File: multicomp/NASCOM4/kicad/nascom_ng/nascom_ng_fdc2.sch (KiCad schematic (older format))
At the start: 32 parts, among them J12 Conn_02x01, J15 Conn_01x04_Male, J16 Conn_01x04_Male, J17 Conn_01x04_Male, J18 Conn_01x04_Male, U14 74LS38, U16 74HCT10, U17 74HCT123, U3 74LS06, U9 74HCT123

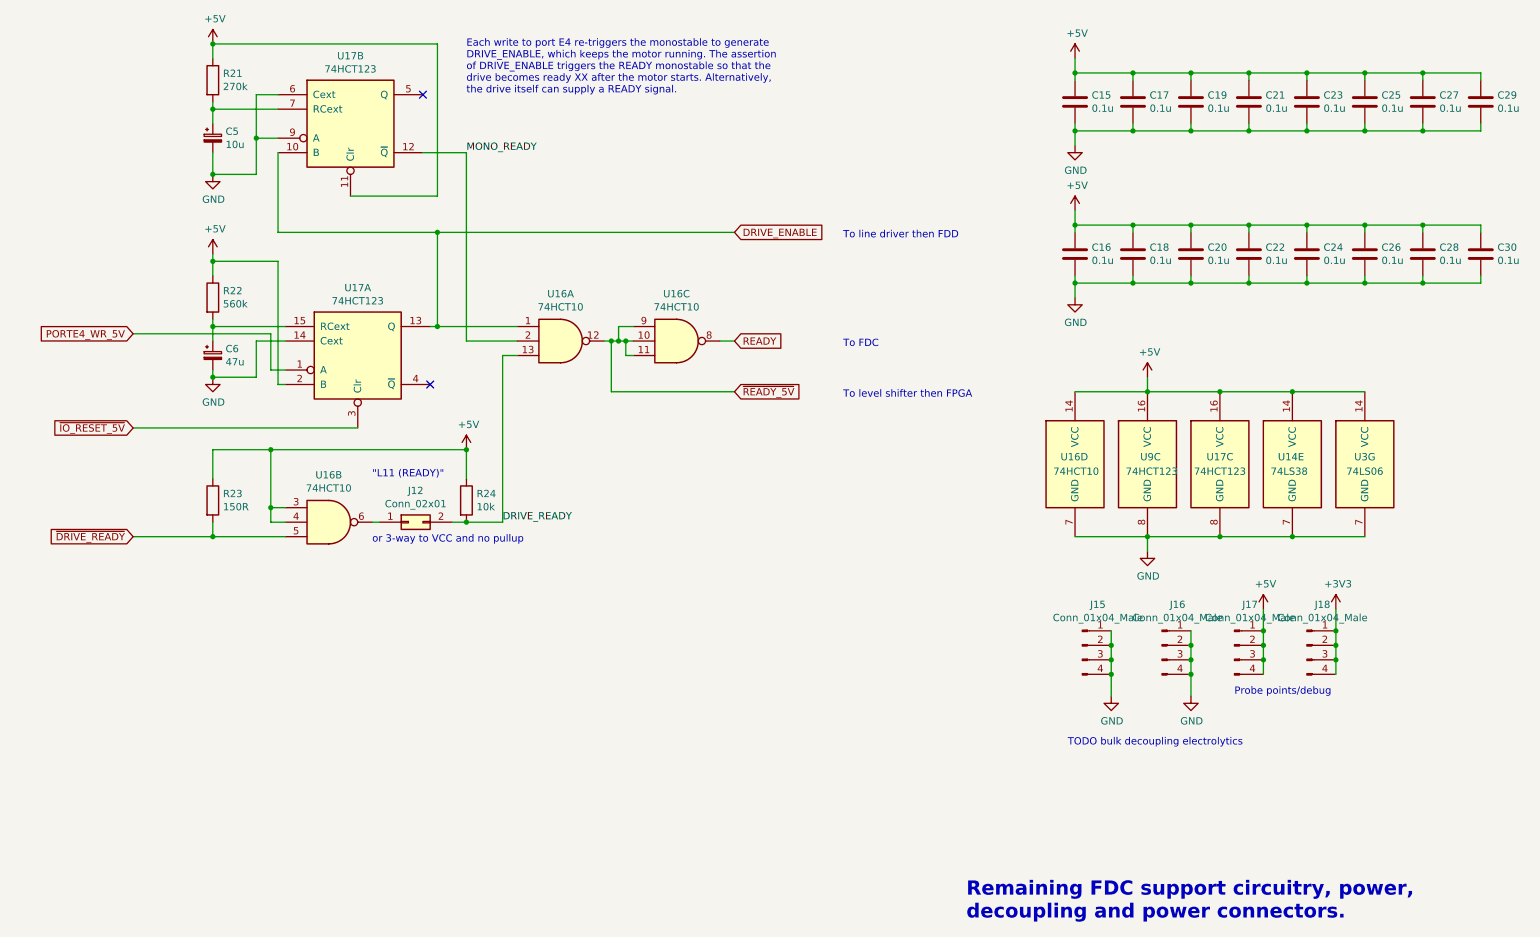
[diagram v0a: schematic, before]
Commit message: All nets routed, ref designators resequenced, nearly finished!
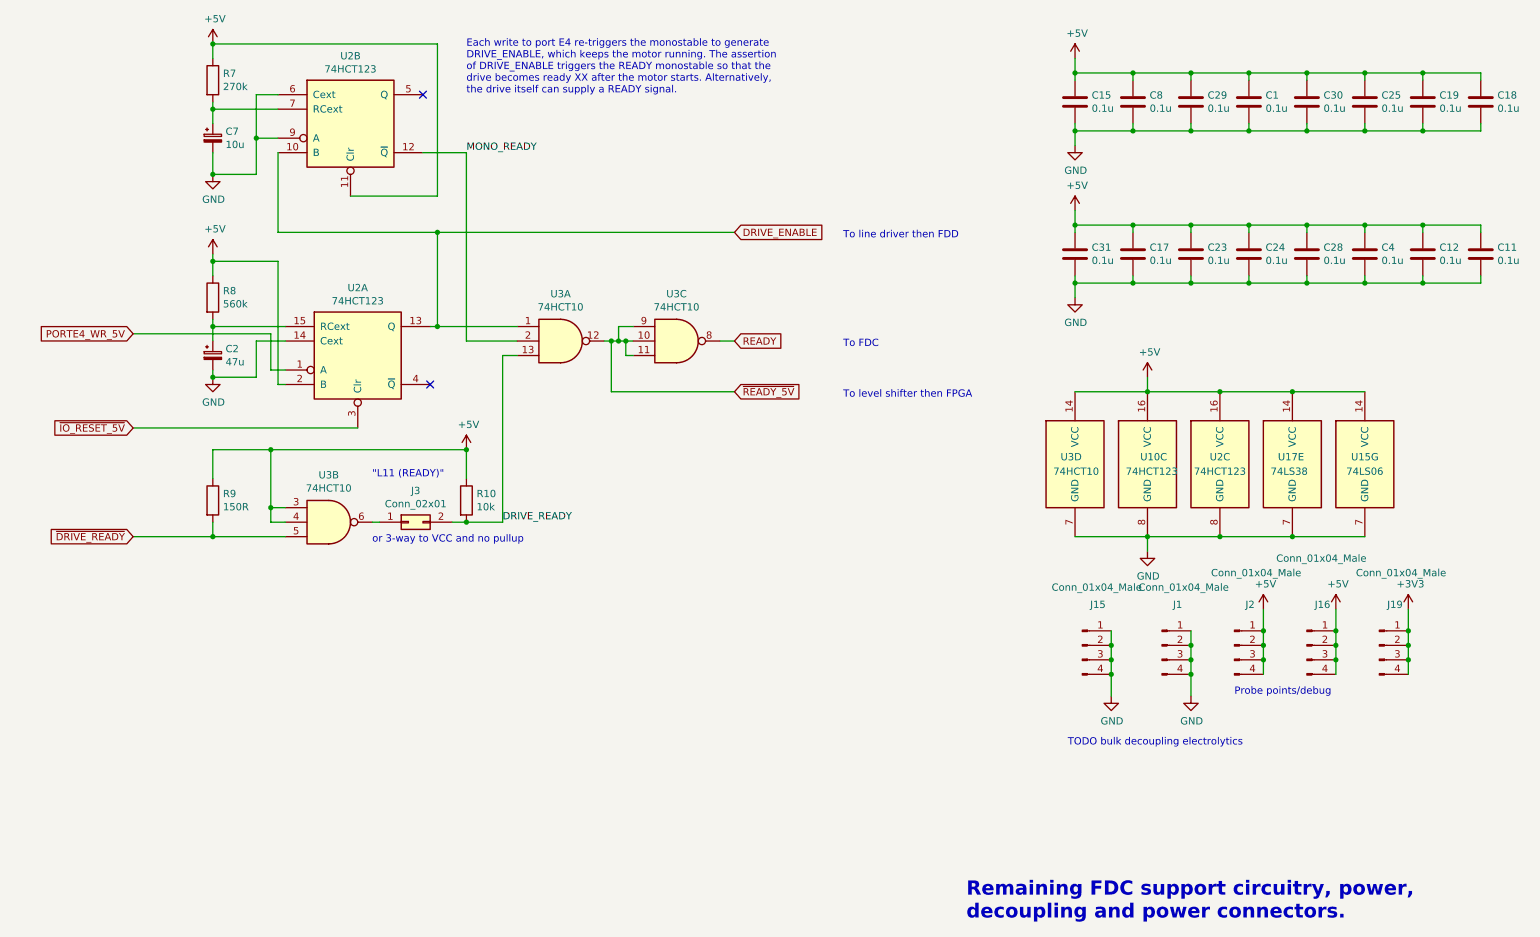
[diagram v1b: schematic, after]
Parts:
- added J16: Conn_01x04_Male, Connector_PinHeader_2.54mm:PinHeader_1x04_P2.54mm_Vertical, symbol Connector:Conn_01x04_Male
- renumbered C21 to C1, C30 to C11, C28 to C12, C18 to C17, C29 to C18, C27 to C19, C6 to C2, C20 to C23, C22 to C24, C24 to C28, C19 to C29, C23 to C30, C16 to C31, C26 to C4, C5 to C7, C17 to C8, J16 to J1, J18 to J19, J17 to J2, J12 to J3, R24 to R10, R21 to R7, R22 to R8, R23 to R9, U9 to U10, U3 to U15, U14 to U17, U17 to U2, U16 to U3
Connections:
- net +5V: now also J16.1 (Pin_1), J16.2 (Pin_2), J16.3 (Pin_3), J16.4 (Pin_4)
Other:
- moved on the sheet: J19

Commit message: Files for REV A release to PCB manufacture
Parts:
- removed C29, C30: 0.1u, Capacitor_THT:C_Disc_D3.0mm_W2.0mm_P2.50mm, symbol Device:C
- added C20, C29: 10u, Capacitor_THT:CP_Radial_D5.0mm_P2.50mm, symbol Device:CP_Small
- renumbered C7 to C10, C11 to C13, C12 to C14, C17 to C16, C15 to C18, C18 to C21, C19 to C23, C23 to C26, C24 to C27, C25 to C28, C28 to C31, C31 to C33, C4 to C5, C2 to C8, C8 to C9, J15 to J14, J16 to J15, J19 to J16, R7 to R6, R10 to R7, U2 to U3, U3 to U4
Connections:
- net +5V: now also C20.1, C29.1
- net GND: now also C20.2, C29.2
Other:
- note removed: "TODO bulk decoupling electrolytics"
- note removed: "or 3-way to VCC and no pullup"

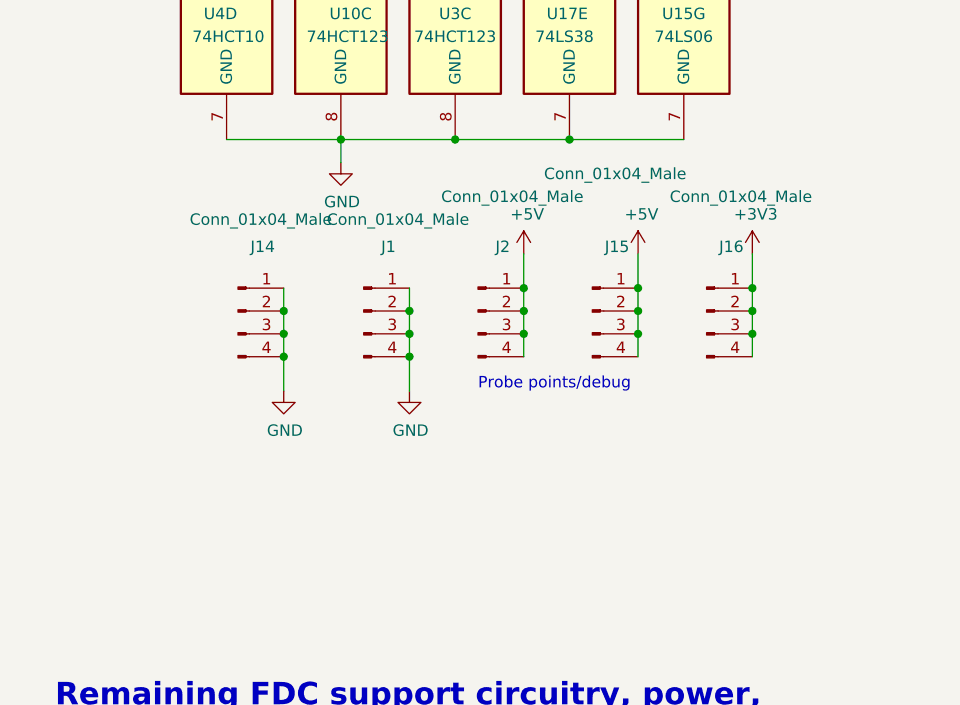
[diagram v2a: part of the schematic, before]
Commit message: Add REVB data-base: schematics, pcb and manufacturing files
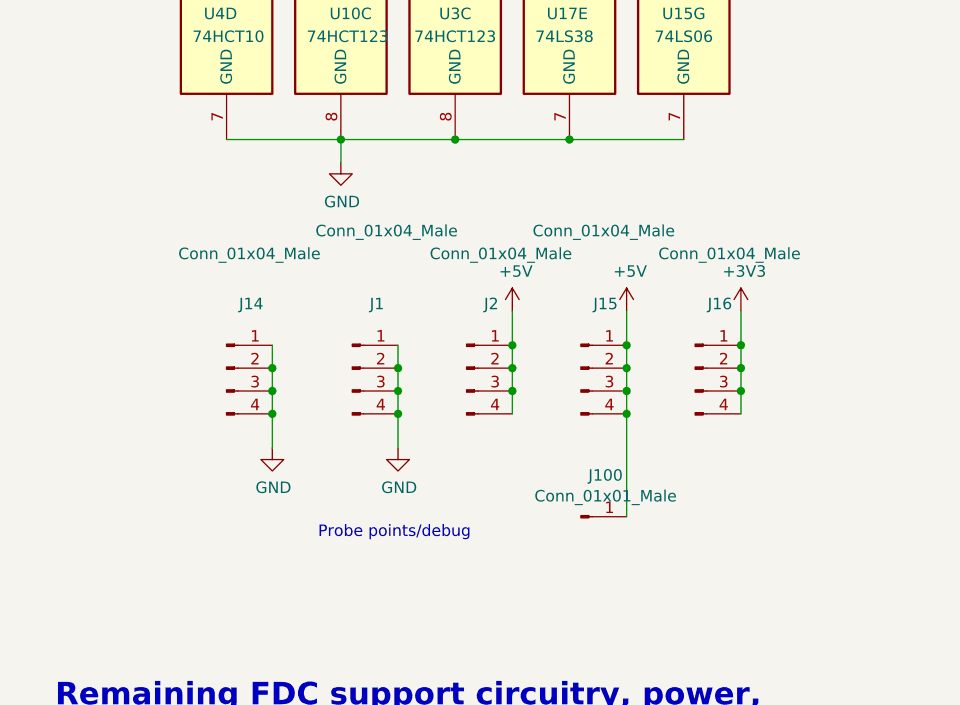
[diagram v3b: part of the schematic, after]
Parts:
- added J100: Conn_01x01_Male, Connector_PinHeader_2.54mm:PinHeader_1x01_P2.54mm_Vertical, symbol Connector:Conn_01x01_Male
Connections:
- net +5V: now also J100.1 (Pin_1)
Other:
- moved on the sheet: J1, J14, J15, J16, J2
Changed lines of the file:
@@
 Sheet 6 6
 Title "NASCOM 4 - a NASCOM in an FPGA"
-Date ""
-Rev ""
+Date "20-Oct-2021"
+Rev "B"
 Comp ""
 Comment1 ""
@@
 L Connector:Conn_01x04_Male J14
 U 1 1 6026C98C
-P 7900 5100
-F 0 "J14" H 8008 5381 50  0000 C CNN
-F 1 "Conn_01x04_Male" H 8000 5500 50  0000 C CNN
-F 2 "Connector_PinHeader_2.54mm:PinHeader_1x04_P2.54mm_Vertical" H 7900 5100 50  0001 C CNN
-F 3 "~" H 7900 5100 50  0001 C CNN
-	1    7900 5100
-	1    0    0    -1
-$EndComp
-Wire Wire Line
-	8100 5000 8100 5100
-Wire Wire Line
-	8100 5100 8100 5200
-Connection ~ 8100 5100
-Wire Wire Line
-	8100 5200 8100 5300
-Connection ~ 8100 5200
-Wire Wire Line
-	8100 5300 8100 5450
-Connection ~ 8100 5300
+P 7850 5350
+F 0 "J14" H 7958 5631 50  0000 C CNN
+F 1 "Conn_01x04_Male" H 7950 5850 50  0000 C CNN
+F 2 "Connector_PinHeader_2.54mm:PinHeader_1x04_P2.54mm_Vertical" H 7850 5350 50  0001 C CNN
+F 3 "~" H 7850 5350 50  0001 C CNN
+	1    7850 5350
+	1    0    0    -1
+$EndComp
+Wire Wire Line
+	8050 5250 8050 5350
+Wire Wire Line
+	8050 5350 8050 5450
+Connection ~ 8050 5350
+Wire Wire Line
+	8050 5450 8050 5550
+Connection ~ 8050 5450
+Wire Wire Line
+	8050 5550 8050 5700
+Connection ~ 8050 5550
 $Comp
 L power:GND #PWR?
 U 1 1 60283F32
-P 8100 5450
+P 8050 5700
 AR Path="/5FC87A4E/60283F32" Ref="#PWR?"  Part="1"
 AR Path="/62588EF4/60283F32" Ref="#PWR0139"  Part="1"
-F 0 "#PWR0139" H 8100 5200 50  0001 C CNN
-F 1 "GND" H 8105 5277 50  0000 C CNN
-F 2 "" H 8100 5450 50  0001 C CNN
-F 3 "" H 8100 5450 50  0001 C CNN
-	1    8100 5450
+F 0 "#PWR0139" H 8050 5450 50  0001 C CNN
+F 1 "GND" H 8055 5527 50  0000 C CNN
+F 2 "" H 8050 5700 50  0001 C CNN
+F 3 "" H 8050 5700 50  0001 C CNN
+	1    8050 5700
 	1    0    0    -1
 $EndComp
@@
 L Connector:Conn_01x04_Male J1
 U 1 1 60287634
-P 8450 5100
-F 0 "J1" H 8558 5381 50  0000 C CNN
-F 1 "Conn_01x04_Male" H 8600 5500 50  0000 C CNN
-F 2 "Connector_PinHeader_2.54mm:PinHeader_1x04_P2.54mm_Vertical" H 8450 5100 50  0001 C CNN
-F 3 "~" H 8450 5100 50  0001 C CNN
-	1    8450 5100
-	1    0    0    -1
-$EndComp
-Wire Wire Line
-	8650 5000 8650 5100
-Wire Wire Line
-	8650 5100 8650 5200
-Connection ~ 8650 5100
-Wire Wire Line
-	8650 5200 8650 5300
-Connection ~ 8650 5200
-Wire Wire Line
-	8650 5300 8650 5450
-Connection ~ 8650 5300
+P 8400 5350
+F 0 "J1" H 8508 5631 50  0000 C CNN
+F 1 "Conn_01x04_Male" H 8550 5950 50  0000 C CNN
+F 2 "Connector_PinHeader_2.54mm:PinHeader_1x04_P2.54mm_Vertical" H 8400 5350 50  0001 C CNN
+F 3 "~" H 8400 5350 50  0001 C CNN
+	1    8400 5350
+	1    0    0    -1
+$EndComp
+Wire Wire Line
+	8600 5250 8600 5350
+Wire Wire Line
+	8600 5350 8600 5450
+Connection ~ 8600 5350
+Wire Wire Line
+	8600 5450 8600 5550
+Connection ~ 8600 5450
+Wire Wire Line
+	8600 5550 8600 5700
+Connection ~ 8600 5550
 $Comp
 L power:GND #PWR?
 U 1 1 60287641
-P 8650 5450
+P 8600 5700
 AR Path="/5FC87A4E/60287641" Ref="#PWR?"  Part="1"
 AR Path="/62588EF4/60287641" Ref="#PWR0140"  Part="1"
-F 0 "#PWR0140" H 8650 5200 50  0001 C CNN
-F 1 "GND" H 8655 5277 50  0000 C CNN
-F 2 "" H 8650 5450 50  0001 C CNN
-F 3 "" H 8650 5450 50  0001 C CNN
-	1    8650 5450
+F 0 "#PWR0140" H 8600 5450 50  0001 C CNN
+F 1 "GND" H 8605 5527 50  0000 C CNN
+F 2 "" H 8600 5700 50  0001 C CNN
+F 3 "" H 8600 5700 50  0001 C CNN
+	1    8600 5700
 	1    0    0    -1
 $EndComp
@@
 L Connector:Conn_01x04_Male J2
 U 1 1 6028CFA0
-P 8950 5100
-F 0 "J2" H 9058 5381 50  0000 C CNN
-F 1 "Conn_01x04_Male" H 9100 5600 50  0000 C CNN
-F 2 "Connector_PinHeader_2.54mm:PinHeader_1x04_P2.54mm_Vertical" H 8950 5100 50  0001 C CNN
-F 3 "~" H 8950 5100 50  0001 C CNN
-	1    8950 5100
-	1    0    0    -1
-$EndComp
-Wire Wire Line
-	9150 5000 9150 5100
-Wire Wire Line
-	9150 5100 9150 5200
-Connection ~ 9150 5100
-Wire Wire Line
-	9150 5200 9150 5300
-Connection ~ 9150 5200
+P 8900 5350
+F 0 "J2" H 9008 5631 50  0000 C CNN
+F 1 "Conn_01x04_Male" H 9050 5850 50  0000 C CNN
+F 2 "Connector_PinHeader_2.54mm:PinHeader_1x04_P2.54mm_Vertical" H 8900 5350 50  0001 C CNN
+F 3 "~" H 8900 5350 50  0001 C CNN
+	1    8900 5350
+	1    0    0    -1
+$EndComp
+Wire Wire Line
+	9100 5250 9100 5350
+Wire Wire Line
+	9100 5350 9100 5450
+Connection ~ 9100 5350
+Wire Wire Line
+	9100 5450 9100 5550
+Connection ~ 9100 5450
 $Comp
 L Connector:Conn_01x04_Male J16
 U 1 1 60292AD5
-P 9950 5100
-F 0 "J16" H 10058 5381 50  0000 C CNN
-F 1 "Conn_01x04_Male" H 10100 5600 50  0000 C CNN
-F 2 "Connector_PinHeader_2.54mm:PinHeader_1x04_P2.54mm_Vertical" H 9950 5100 50  0001 C CNN
-F 3 "~" H 9950 5100 50  0001 C CNN
-	1    9950 5100
-	1    0    0    -1
-$EndComp
-Wire Wire Line
-	10150 5000 10150 5100
-Wire Wire Line
-	10150 5100 10150 5200
-Connection ~ 10150 5100
-Wire Wire Line
-	10150 5200 10150 5300
-Connection ~ 10150 5200
+P 9900 5350
+F 0 "J16" H 10008 5631 50  0000 C CNN
+F 1 "Conn_01x04_Male" H 10050 5850 50  0000 C CNN
+F 2 "Connector_PinHeader_2.54mm:PinHeader_1x04_P2.54mm_Vertical" H 9900 5350 50  0001 C CNN
+F 3 "~" H 9900 5350 50  0001 C CNN
+	1    9900 5350
+	1    0    0    -1
+$EndComp
+Wire Wire Line
+	10100 5250 10100 5350
+Wire Wire Line
+	10100 5350 10100 5450
+Connection ~ 10100 5350
+Wire Wire Line
+	10100 5450 10100 5550
+Connection ~ 10100 5450
 $Comp
 L power:+5V #PWR?
 U 1 1 60299B58
-P 9150 4850
+P 9100 5100
 AR Path="/5FC87A4E/60299B58" Ref="#PWR?"  Part="1"
 AR Path="/62588EF4/60299B58" Ref="#PWR0141"  Part="1"
-F 0 "#PWR0141" H 9150 4700 50  0001 C CNN
-F 1 "+5V" H 9165 5023 50  0000 C CNN
-F 2 "" H 9150 4850 50  0001 C CNN
-F 3 "" H 9150 4850 50  0001 C CNN
-	1    9150 4850
+F 0 "#PWR0141" H 9100 4950 50  0001 C CNN
+F 1 "+5V" H 9115 5273 50  0000 C CNN
+F 2 "" H 9100 5100 50  0001 C CNN
+F 3 "" H 9100 5100 50  0001 C CNN
+	1    9100 5100
 	1    0    0    -1
 $EndComp
@@
 L power:+3V3 #PWR0142
 U 1 1 6029D69A
-P 10150 4850
-F 0 "#PWR0142" H 10150 4700 50  0001 C CNN
-F 1 "+3V3" H 10165 5023 50  0000 C CNN
-F 2 "" H 10150 4850 50  0001 C CNN
-F 3 "" H 10150 4850 50  0001 C CNN
-	1    10150 4850
-	1    0    0    -1
-$EndComp
-Wire Wire Line
-	10150 5000 10150 4850
-Connection ~ 10150 5000
-Wire Wire Line
-	9150 5000 9150 4850
-Connection ~ 9150 5000
-Text Notes 8950 5450 0    50   ~ 0
+P 10100 5100
+F 0 "#PWR0142" H 10100 4950 50  0001 C CNN
+F 1 "+3V3" H 10115 5273 50  0000 C CNN
+F 2 "" H 10100 5100 50  0001 C CNN
+F 3 "" H 10100 5100 50  0001 C CNN
+	1    10100 5100
+	1    0    0    -1
+$EndComp
+Wire Wire Line
+	10100 5250 10100 5100
+Connection ~ 10100 5250
+Wire Wire Line
+	9100 5250 9100 5100
+Connection ~ 9100 5250
+Text Notes 8250 6100 0    50   ~ 0
 Probe points/debug
-Connection ~ 9650 5000
-Wire Wire Line
-	9650 5000 9650 4850
+Connection ~ 9600 5250
+Wire Wire Line
+	9600 5250 9600 5100
 $Comp
 L power:+5V #PWR?
 U 1 1 603F445D
-P 9650 4850
+P 9600 5100
 AR Path="/5FC87A4E/603F445D" Ref="#PWR?"  Part="1"
 AR Path="/62588EF4/603F445D" Ref="#PWR042"  Part="1"
-F 0 "#PWR042" H 9650 4700 50  0001 C CNN
-F 1 "+5V" H 9665 5023 50  0000 C CNN
-F 2 "" H 9650 4850 50  0001 C CNN
-F 3 "" H 9650 4850 50  0001 C CNN
-	1    9650 4850
-	1    0    0    -1
-$EndComp
-Connection ~ 9650 5200
-Wire Wire Line
-	9650 5200 9650 5300
-Connection ~ 9650 5100
-Wire Wire Line
-	9650 5100 9650 5200
-Wire Wire Line
-	9650 5000 9650 5100
+F 0 "#PWR042" H 9600 4950 50  0001 C CNN
+F 1 "+5V" H 9615 5273 50  0000 C CNN
+F 2 "" H 9600 5100 50  0001 C CNN
+F 3 "" H 9600 5100 50  0001 C CNN
+	1    9600 5100
+	1    0    0    -1
+$EndComp
+Connection ~ 9600 5450
+Wire Wire Line
+	9600 5450 9600 5550
+Connection ~ 9600 5350
+Wire Wire Line
+	9600 5350 9600 5450
+Wire Wire Line
+	9600 5250 9600 5350
 $Comp
 L Connector:Conn_01x04_Male J15
 U 1 1 603F4452
-P 9450 5100
-F 0 "J15" H 9558 5381 50  0000 C CNN
-F 1 "Conn_01x04_Male" H 9550 5700 50  0000 C CNN
-F 2 "Connector_PinHeader_2.54mm:PinHeader_1x04_P2.54mm_Vertical" H 9450 5100 50  0001 C CNN
-F 3 "~" H 9450 5100 50  0001 C CNN
-	1    9450 5100
+P 9400 5350
+F 0 "J15" H 9508 5631 50  0000 C CNN
+F 1 "Conn_01x04_Male" H 9500 5950 50  0000 C CNN
+F 2 "Connector_PinHeader_2.54mm:PinHeader_1x04_P2.54mm_Vertical" H 9400 5350 50  0001 C CNN
+F 3 "~" H 9400 5350 50  0001 C CNN
+	1    9400 5350
 	1    0    0    -1
 $EndComp
@@
 Wire Wire Line
 	8650 1150 8650 1250
+$Comp
+L Connector:Conn_01x01_Male J100
+U 1 1 6177D3FE
+P 9400 6000
+F 0 "J100" H 9508 6181 50  0000 C CNN
+F 1 "Conn_01x01_Male" H 9508 6090 50  0000 C CNN
+F 2 "Connector_PinHeader_2.54mm:PinHeader_1x01_P2.54mm_Vertical" H 9400 6000 50  0001 C CNN
+F 3 "~" H 9400 6000 50  0001 C CNN
+	1    9400 6000
+	1    0    0    -1
+$EndComp
+Wire Wire Line
+	9600 5550 9600 6000
+Connection ~ 9600 5550
 $EndSCHEMATC
